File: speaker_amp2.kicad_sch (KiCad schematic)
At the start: 72 parts, among them J1 Molex_430450227, J2 Molex_430450227, J3 Molex_430450227, J4 Molex_430450227, J5 Molex_1053101106, U1 TAS5822MDCPR, U2 TAS5822MDCPR

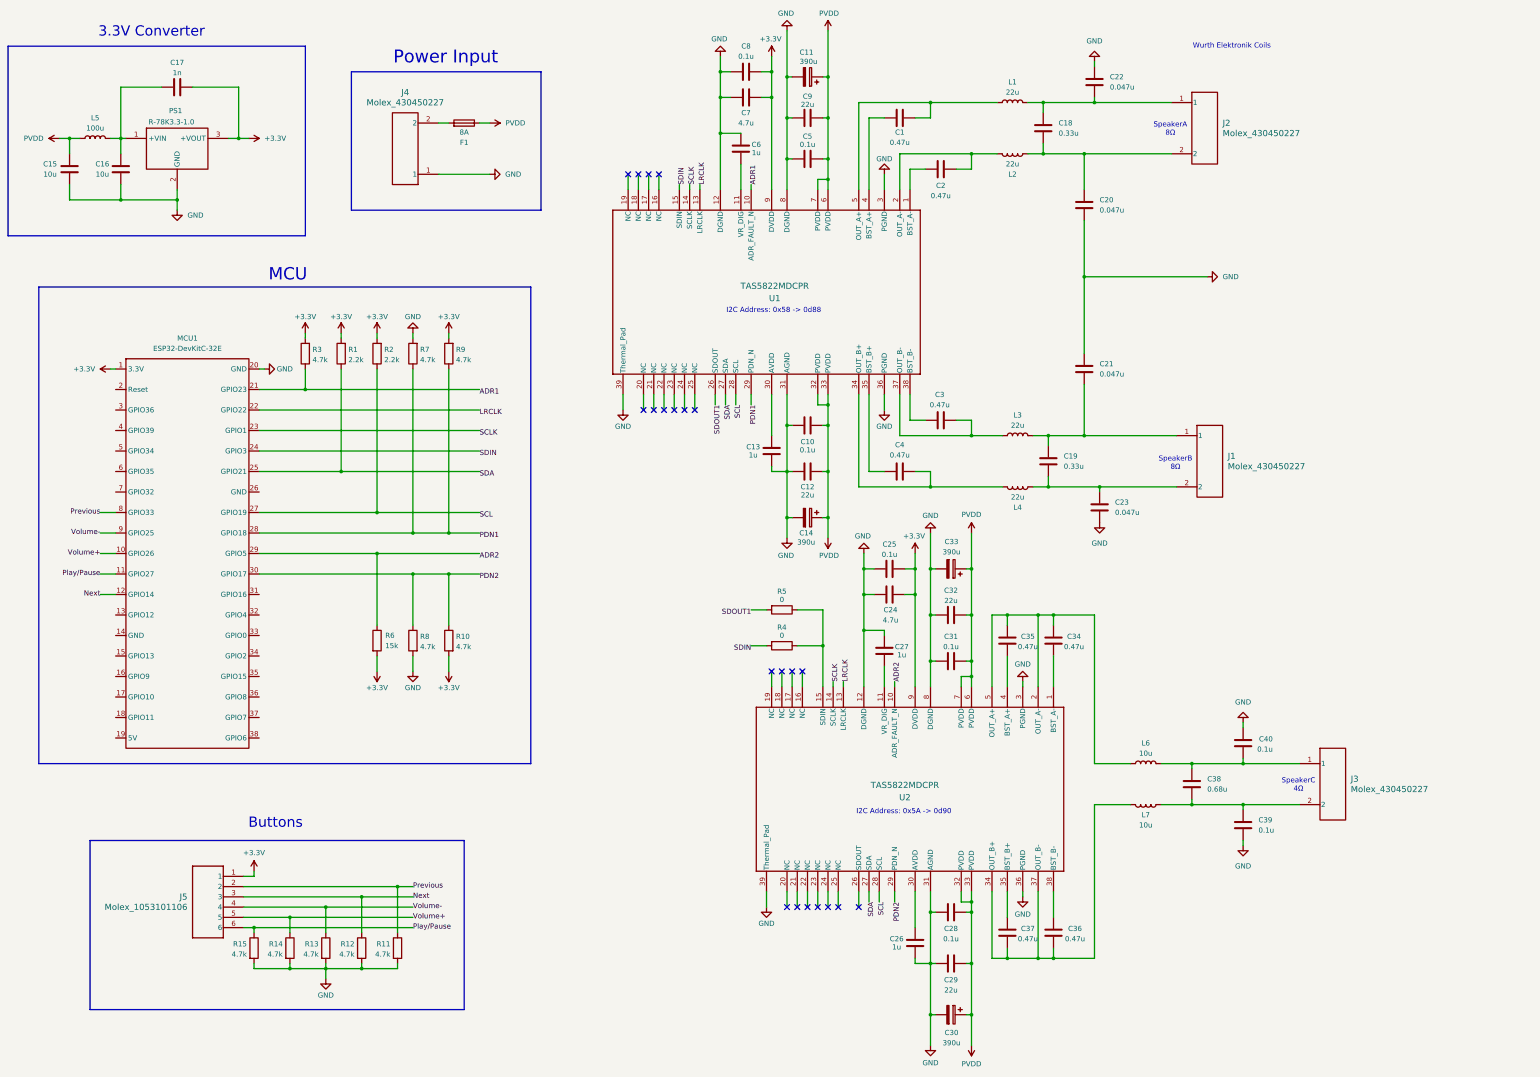
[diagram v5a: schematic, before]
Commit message: changed some components (coils) for smaller ones
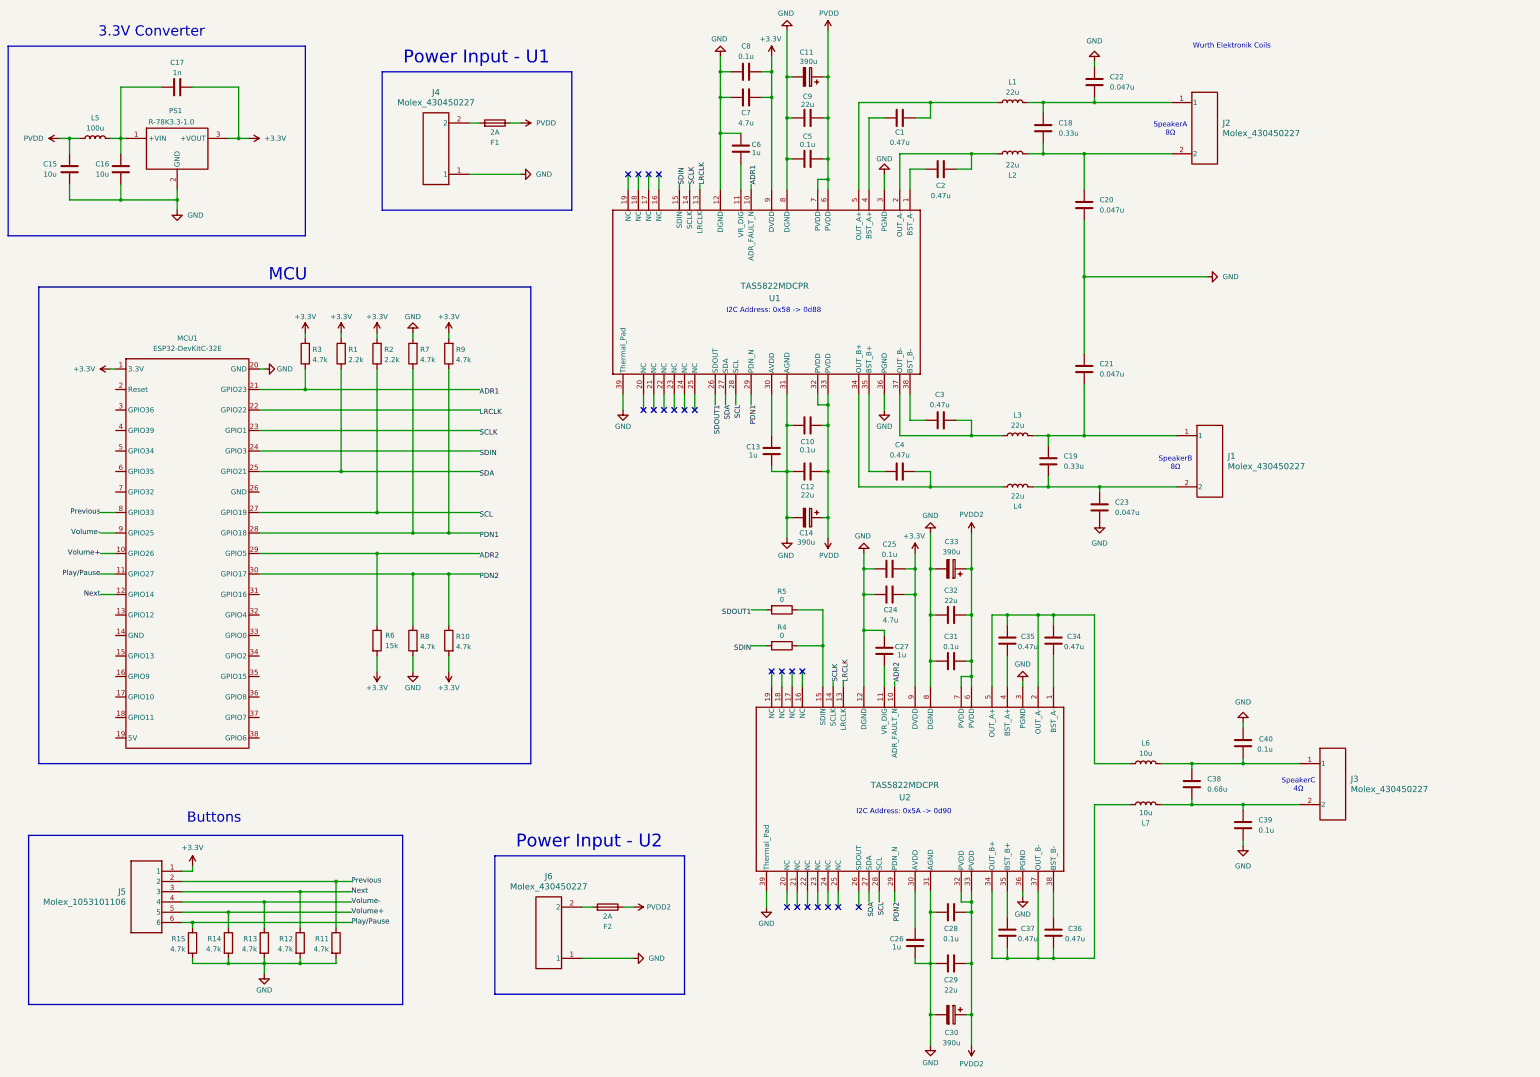
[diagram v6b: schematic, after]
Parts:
- added F2: 2A, Fuse:Fuse_1206_3216Metric, symbol Device:Fuse
- added J6: Molex_430450227, Speaker Amp Lib:430450227_MOLEX, symbol Speaker Amp Lib:Molex_430450227
- F1: value 8A -> 2A; MouserLink https://gr.mouser.com/ProductDetail/Bel-Fuse/0685P8000-01?q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 -> https://gr.mouser.com/ProductDetail/Bel-Fuse/0685P2000-01?q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
- L1, L2, L3, L4: footprint Inductor_SMD:L_Wuerth_WE-PD-Typ-LS_Handsoldering -> Inductor_SMD:L_Wuerth_WE-PD-Typ-M-Typ-S_Handsoldering; MouserLink https://gr.mouser.com/ProductDetail/Wurth-Elektronik/744770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 -> https://gr.mouser.com/ProductDetail/Wurth-Elektronik/744777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
- L6, L7: footprint Inductor_SMD:L_Wuerth_WE-PD-Typ-LS_Handsoldering -> Speaker Amp Lib:L_Wuerth_WE-PDF_Handsoldering_7mm_apart; MouserLink https://gr.mouser.com/ProductDetail/Wurth-Elektronik/744770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 -> https://gr.mouser.com/ProductDetail/Wurth-Elektronik/744771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
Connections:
- net GND: now also J6.1
- net PVDD: no longer C28.1, C29.1, C30.1, C31.1, C32.1, C33.1, U2.32 (PVDD), U2.33 (PVDD), U2.6 (PVDD), U2.7 (PVDD)
- net at C19.2, C23.1, J1.2: now also L4.2; no longer L4.1
- net at C38.2, C39.1, J3.2: now also L7.2; no longer L7.1
- net at C18.2, C20.1, J2.2: now also L2.2; no longer L2.1
- net at C2.2, U1.2 (OUT_A-): now also L2.1; no longer L2.2
- net at C4.2, U1.34 (OUT_B+): now also L4.1; no longer L4.2
- net at C36.2, C37.2, U2.34 (OUT_B+)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: now also L7.1; no longer L7.2
- new net: F2.2, J6.2
- new net PVDD2: C28.1, C29.1, C30.1, C31.1, C32.1, C33.1, F2.1, U2.32 (PVDD), U2.33 (PVDD), U2.6 (PVDD), U2.7 (PVDD)
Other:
- note added: "Power Input - U1"
- note added: "Power Input - U2"
- note removed: "Power Input"
- moved on the sheet: J4, J5, R11, R12, R13, R14, R15

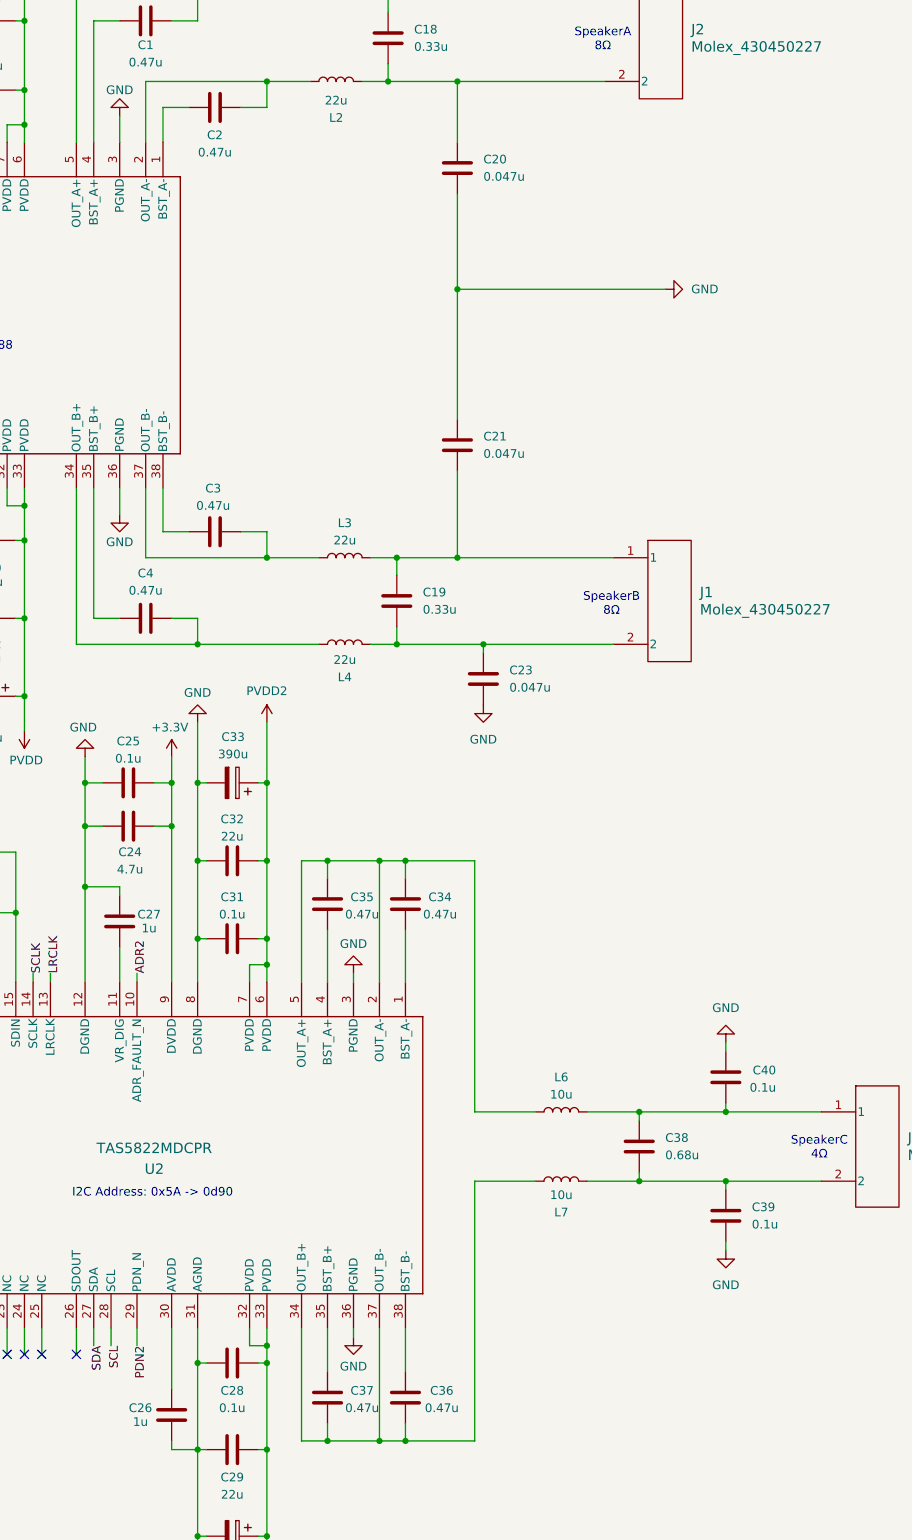
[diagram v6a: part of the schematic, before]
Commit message: changed output capacitors to smaller ones
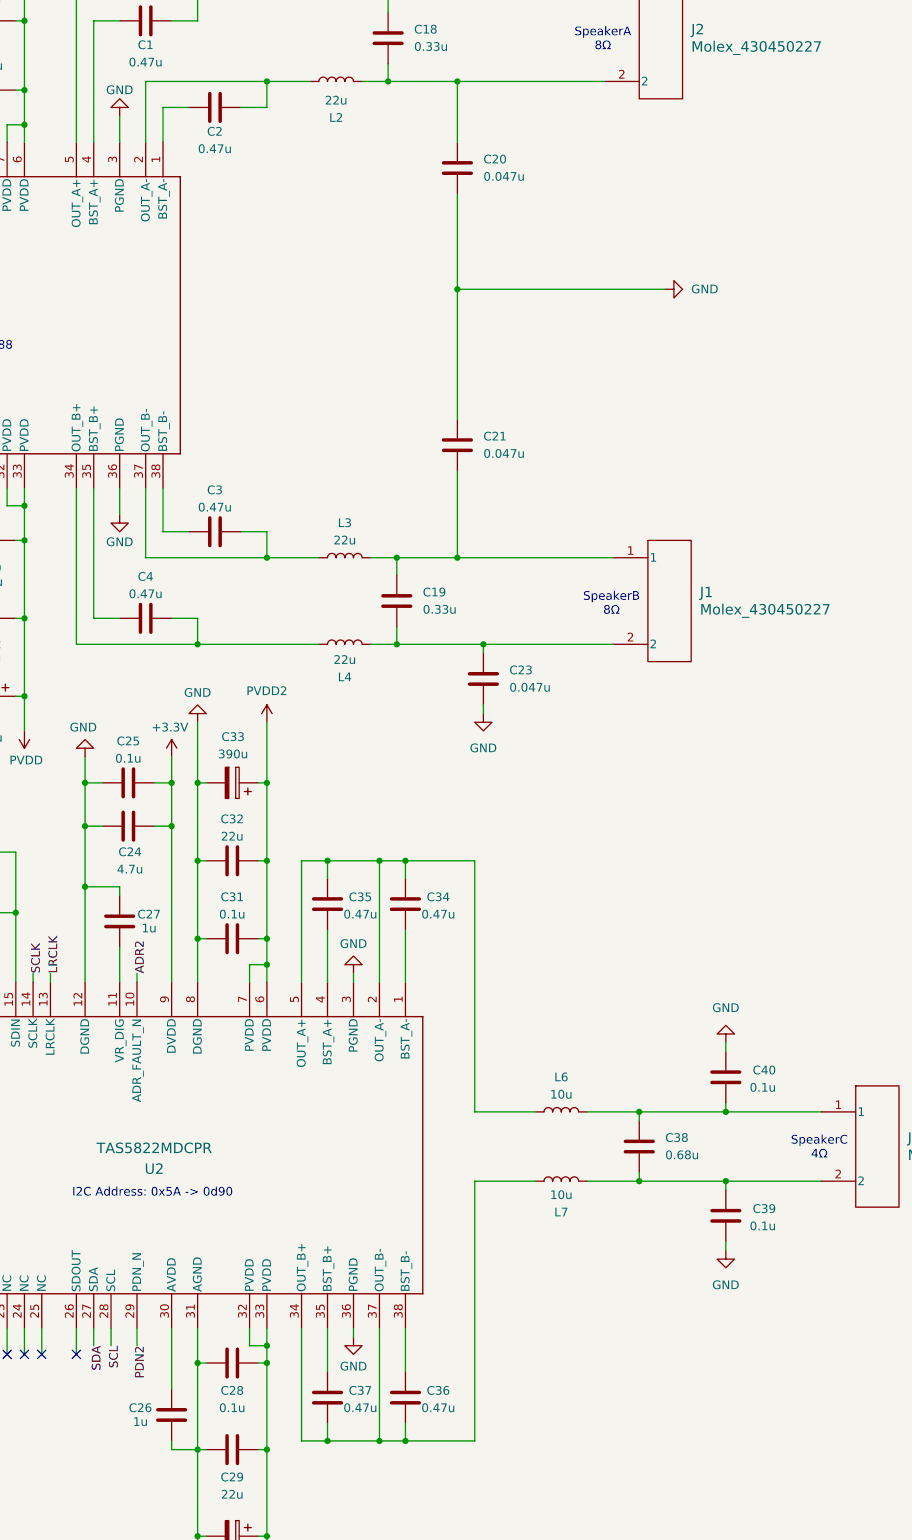
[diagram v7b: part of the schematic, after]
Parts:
- C1, C2, C3, C34, C35, C36, C37, C4: footprint Capacitor_SMD:C_0805_2012Metric_Pad1.18x1.45mm_HandSolder -> Capacitor_SMD:C_0603_1608Metric_Pad1.08x0.95mm_HandSolder; MouserLink https://gr.mouser.com/ProductDetail/KEMET/C0805C474J5RECTU?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 -> https://gr.mouser.com/ProductDetail/TAIYO-YUDEN/MLASU168SB7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
- C18, C19: footprint Capacitor_THT:C_Rect_L18.0mm_W9.0mm_P15.00mm_FKS3_FKP3 -> Speaker Amp Lib:C_2824; MouserLink https://gr.mouser.com/ProductDetail/KEMET/R75MI333050H4J?qs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 -> https://gr.mouser.com/ProductDetail/WIMA/SMD2824-.33-100-10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
- C20, C21, C22, C23: footprint Capacitor_THT:C_Rect_L13.0mm_W5.0mm_P10.00mm_FKS3_FKP3_MKS4 -> Capacitor_SMD:C_2220_5750Metric_Pad1.97x5.40mm_HandSolder; MouserLink https://gr.mouser.com/ProductDetail/KEMET/R76MF24705050J?qs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 -> https://gr.mouser.com/ProductDetail/WIMA/SMDTD02470QA00KP00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
- C38: footprint Speaker Amp Lib:C_Rect_L18.0mm_W13.0mm_P15.00mm_FKS3_FKP3 -> Speaker Amp Lib:C_2824; MouserLink https://gr.mouser.com/ProductDetail/KEMET/R75II368050H8J?qs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 -> https://gr.mouser.com/ProductDetail/WIMA/SMDIC03680TB00KQ00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
- C39, C40: footprint Capacitor_THT:C_Rect_L18.0mm_W5.0mm_P15.00mm_FKS3_FKP3 -> Capacitor_SMD:C_2220_5750Metric_Pad1.97x5.40mm_HandSolder; MouserLink https://gr.mouser.com/ProductDetail/KEMET/R75MI3100AA30K?qs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 -> https://gr.mouser.com/ProductDetail/WIMA/SMDTD03100QA00KP00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
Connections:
- net GND: now also C39.1; no longer C39.2
- net at C38.2, J3.2, L7.2: now also C39.2; no longer C39.1
- net at L6.1, U2.2 (OUT_A-), U2.5 (OUT_A+): now also C34.2, C35.2; no longer C34.1, C35.1
- net at U2.4 (BST_A+): now also C35.1; no longer C35.2
- net at L7.1, U2.34 (OUT_B+), U2.37 (OUT_B-): now also C36.1, C37.1; no longer C36.2, C37.2
- net at U2.38 (BST_B-): now also C36.2; no longer C36.1
- net at U2.35 (BST_B+): now also C37.2; no longer C37.1
- net at U2.1 (BST_A-): now also C34.1; no longer C34.2

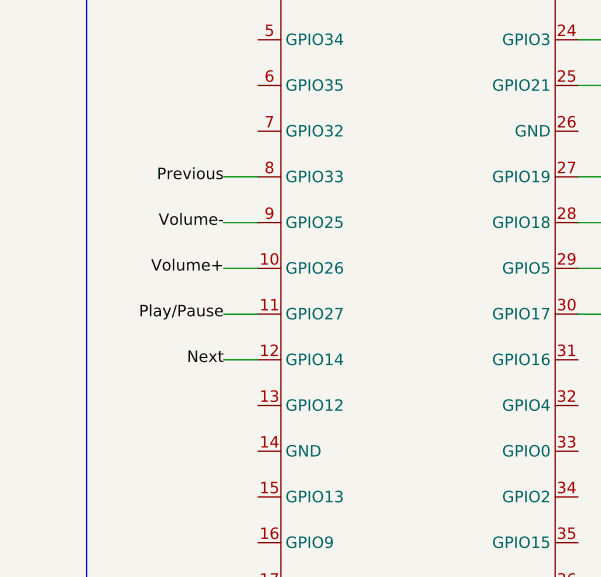
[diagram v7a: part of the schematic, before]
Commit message: finalized pcb component placement; started connections
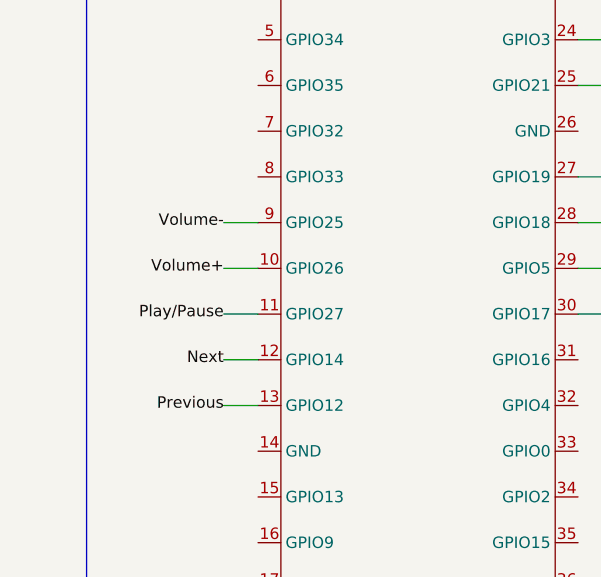
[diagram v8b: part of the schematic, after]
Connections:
- net Previous: now also MCU1.13 (GPIO12); no longer MCU1.8 (GPIO33)
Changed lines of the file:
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@@
 	(wire
 		(pts
-			(xy 45.72 140.97) (xy 49.53 140.97)
-		)
-		(stroke
-			(width 0)
-			(type default)
-		)
-	)
-	(wire
-		(pts
 			(xy 251.46 43.18) (xy 251.46 39.37)
 		)
@@
 	(wire
 		(pts
+			(xy 45.72 146.05) (xy 49.53 146.05)
+		)
+		(stroke
+			(width 0)
+			(type default)
+		)
+	)
+	(wire
+		(pts
 			(xy 266.7 166.37) (xy 270.51 166.37)
 		)
@@
 	(wire
 		(pts
+			(xy 45.72 166.37) (xy 49.53 166.37)
+		)
+		(stroke
+			(width 0)
+			(type default)
+		)
+	)
+	(wire
+		(pts
 			(xy 328.93 213.36) (xy 342.9 213.36)
 		)
@@
 	(wire
 		(pts
-			(xy 261.62 265.43) (xy 261.62 273.05)
+			(xy 45.72 151.13) (xy 49.53 151.13)
 		)
 		(stroke
@@
 	(wire
 		(pts
-			(xy 200.66 111.76) (xy 200.66 114.3)
+			(xy 261.62 265.43) (xy 261.62 273.05)
 		)
 		(stroke
@@
 	(wire
 		(pts
-			(xy 278.13 251.46) (xy 281.94 251.46)
+			(xy 200.66 111.76) (xy 200.66 114.3)
 		)
 		(stroke
@@
 	(wire
 		(pts
-			(xy 316.23 213.36) (xy 328.93 213.36)
+			(xy 278.13 251.46) (xy 281.94 251.46)
 		)
 		(stroke
@@
 	(wire
 		(pts
-			(xy 68.58 243.84) (xy 68.58 242.57)
+			(xy 316.23 213.36) (xy 328.93 213.36)
 		)
 		(stroke
@@
 	(wire
 		(pts
-			(xy 266.7 184.15) (xy 266.7 166.37)
+			(xy 68.58 243.84) (xy 68.58 242.57)
 		)
 		(stroke
@@
 	(wire
 		(pts
-			(xy 215.9 142.24) (xy 215.9 147.32)
+			(xy 266.7 184.15) (xy 266.7 166.37)
 		)
 		(stroke
@@
 	(wire
 		(pts
-			(xy 45.72 156.21) (xy 49.53 156.21)
+			(xy 215.9 142.24) (xy 215.9 147.32)
 		)
 		(stroke
@@
 	(wire
 		(pts
+			(xy 45.72 161.29) (xy 49.53 161.29)
+		)
+		(stroke
+			(width 0)
+			(type default)
+		)
+	)
+	(wire
+		(pts
 			(xy 223.52 58.42) (xy 226.06 58.42)
 		)
@@
 	(wire
 		(pts
-			(xy 45.72 151.13) (xy 49.53 151.13)
-		)
-		(stroke
-			(width 0)
-			(type default)
-		)
-	)
-	(wire
-		(pts
 			(xy 243.84 121.92) (xy 243.84 111.76)
 		)
@@
 	(wire
 		(pts
-			(xy 45.72 146.05) (xy 49.53 146.05)
-		)
-		(stroke
-			(width 0)
-			(type default)
-		)
-	)
-	(wire
-		(pts
 			(xy 114.3 105.41) (xy 114.3 140.97)
 		)
@@
 	(wire
 		(pts
-			(xy 45.72 161.29) (xy 49.53 161.29)
-		)
-		(stroke
-			(width 0)
-			(type default)
-		)
-	)
-	(wire
-		(pts
 			(xy 132.08 180.34) (xy 132.08 176.53)
 		)
@@
 	(wire
 		(pts
+			(xy 45.72 156.21) (xy 49.53 156.21)
+		)
+		(stroke
+			(width 0)
+			(type default)
+		)
+	)
+	(wire
+		(pts
 			(xy 85.09 120.65) (xy 139.7 120.65)
 		)
@@
 		)
 	)
-	(label "Volume-"
-		(at 45.72 146.05 180)
-		(fields_autoplaced yes)
-		(effects
-			(font
-				(size 1.27 1.27)
-			)
-			(justify right)
-		)
-	)
 	(label "PDN2"
 		(at 139.7 156.21 0)
@@
 		)
 	)
+	(label "Volume-"
+		(at 45.72 146.05 180)
+		(fields_autoplaced yes)
+		(effects
+			(font
+				(size 1.27 1.27)
+			)
+			(justify right)
+		)
+	)
 	(label "PDN2"
 		(at 242.57 237.49 270)
@@
 	)
 	(label "Previous"
-		(at 45.72 140.97 180)
+		(at 45.72 166.37 180)
 		(fields_autoplaced yes)
 		(effects
